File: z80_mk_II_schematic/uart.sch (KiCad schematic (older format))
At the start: 20 parts

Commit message: Lots more work on schematic
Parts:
- U22: renamed from U?; value 74LS32 -> 74LS365
- U24: renamed from U?; value 74LS32 -> D3-6402
- U25: renamed from U?; value 74LS32 -> 74LS139
- U27: renamed from U?; value 74LS32 -> MAX232
- gave numbers to parts that had none: 12
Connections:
- net ~UART_EN~ renamed ~UART_CE~

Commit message: Un-fsck something which made most of the chips into 74LS00 for some very odd reason. Also start to assign footprints.
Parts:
- R24: footprint (none) -> Resistors_ThroughHole:R_Axial_DIN0207_L6.3mm_D2.5mm_P10.16mm_Horizontal
- U22, U25: footprint (none) -> Housings_DIP:DIP-16_W7.62mm
- U23, U26: footprint (none) -> Housings_DIP:DIP-14_W7.62mm
- U24: footprint (none) -> Housings_DIP:DIP-40_W15.24mm_Socket
- U27: footprint (none) -> Housings_DIP:DIP-20_W7.62mm_Socket
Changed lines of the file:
@@
 F 0 "U24" H 5500 3800 50  0000 C CNN
 F 1 "D3-6402" H 5500 3700 50  0000 C CNN
-F 2 "" H 5500 2400 50  0001 C CNN
+F 2 "Housings_DIP:DIP-40_W15.24mm_Socket" H 5500 2400 50  0001 C CNN
 F 3 "" H 5450 2200 50  0001 C CNN
 	1    5500 3800
@@
 F 0 "U27" H 9100 3350 50  0000 C CNN
 F 1 "MAX232" H 9100 3250 50  0000 C CNN
-F 2 "" H 9200 1900 50  0001 L CNN
+F 2 "Housings_DIP:DIP-20_W7.62mm_Socket" H 9200 1900 50  0001 L CNN
 F 3 "" H 9150 3050 50  0001 C CNN
 	1    9150 2950
@@
 F 0 "U25" H 5500 5900 50  0000 C CNN
 F 1 "74LS139" H 5450 5800 50  0000 C CNN
-F 2 "" H 5500 5900 50  0001 C CNN
+F 2 "Housings_DIP:DIP-16_W7.62mm" H 5500 5900 50  0001 C CNN
 F 3 "" H 5500 5900 50  0001 C CNN
 	1    5500 5900
@@
 F 0 "U25" H 5500 6800 50  0000 C CNN
 F 1 "74LS139" H 5450 6700 50  0000 C CNN
-F 2 "" H 5500 6800 50  0001 C CNN
+F 2 "Housings_DIP:DIP-16_W7.62mm" H 5500 6800 50  0001 C CNN
 F 3 "" H 5500 6800 50  0001 C CNN
 	2    5500 6800
@@
 F 0 "U25" H 8980 5896 50  0000 L CNN
 F 1 "74LS139" H 8980 5805 50  0000 L CNN
-F 2 "" H 8750 5850 50  0001 C CNN
+F 2 "Housings_DIP:DIP-16_W7.62mm" H 8750 5850 50  0001 C CNN
 F 3 "" H 8750 5850 50  0001 C CNN
 	3    8750 5850
@@
 F 0 "U23" H 4200 6800 50  0000 C CNN
 F 1 "74LS32" H 4200 7034 50  0000 C CNN
-F 2 "" H 4200 6800 50  0001 C CNN
+F 2 "Housings_DIP:DIP-14_W7.62mm" H 4200 6800 50  0001 C CNN
 F 3 "http://www.ti.com/lit/gpn/sn74LS32" H 4200 6800 50  0001 C CNN
 	1    4200 6800
@@
 F 0 "U22" H 3150 4300 50  0000 C CNN
 F 1 "74LS365" H 3150 4200 50  0000 C CNN
-F 2 "" H 3150 4400 50  0001 C CNN
+F 2 "Housings_DIP:DIP-16_W7.62mm" H 3150 4400 50  0001 C CNN
 F 3 "" H 3150 4400 50  0001 C CNN
 	1    3150 4400
@@
 F 0 "R24" V 3554 5650 50  0000 C CNN
 F 1 "10K" V 3645 5650 50  0000 C CNN
-F 2 "" H 3750 5650 50  0001 C CNN
+F 2 "Resistors_ThroughHole:R_Axial_DIN0207_L6.3mm_D2.5mm_P10.16mm_Horizontal" H 3750 5650 50  0001 C CNN
 F 3 "~" H 3750 5650 50  0001 C CNN
 	1    3750 5650
@@
 F 0 "U23" H 4200 7350 50  0000 C CNN
 F 1 "74LS32" H 4200 7584 50  0000 C CNN
-F 2 "" H 4200 7350 50  0001 C CNN
+F 2 "Housings_DIP:DIP-14_W7.62mm" H 4200 7350 50  0001 C CNN
 F 3 "http://www.ti.com/lit/gpn/sn74LS32" H 4200 7350 50  0001 C CNN
 	4    4200 7350
@@
 F 0 "U23" H 9780 5896 50  0000 L CNN
 F 1 "74LS32" H 9780 5805 50  0000 L CNN
-F 2 "" H 9550 5850 50  0001 C CNN
+F 2 "Housings_DIP:DIP-14_W7.62mm" H 9550 5850 50  0001 C CNN
 F 3 "http://www.ti.com/lit/gpn/sn74LS32" H 9550 5850 50  0001 C CNN
 	5    9550 5850
@@
 F 0 "U26" V 6450 6100 50  0000 R CNN
 F 1 "74LS00" H 6550 5750 50  0000 R CNN
-F 2 "" H 6450 6000 50  0001 C CNN
+F 2 "Housings_DIP:DIP-14_W7.62mm" H 6450 6000 50  0001 C CNN
 F 3 "http://www.ti.com/lit/gpn/sn74ls00" H 6450 6000 50  0001 C CNN
 	3    6450 6000

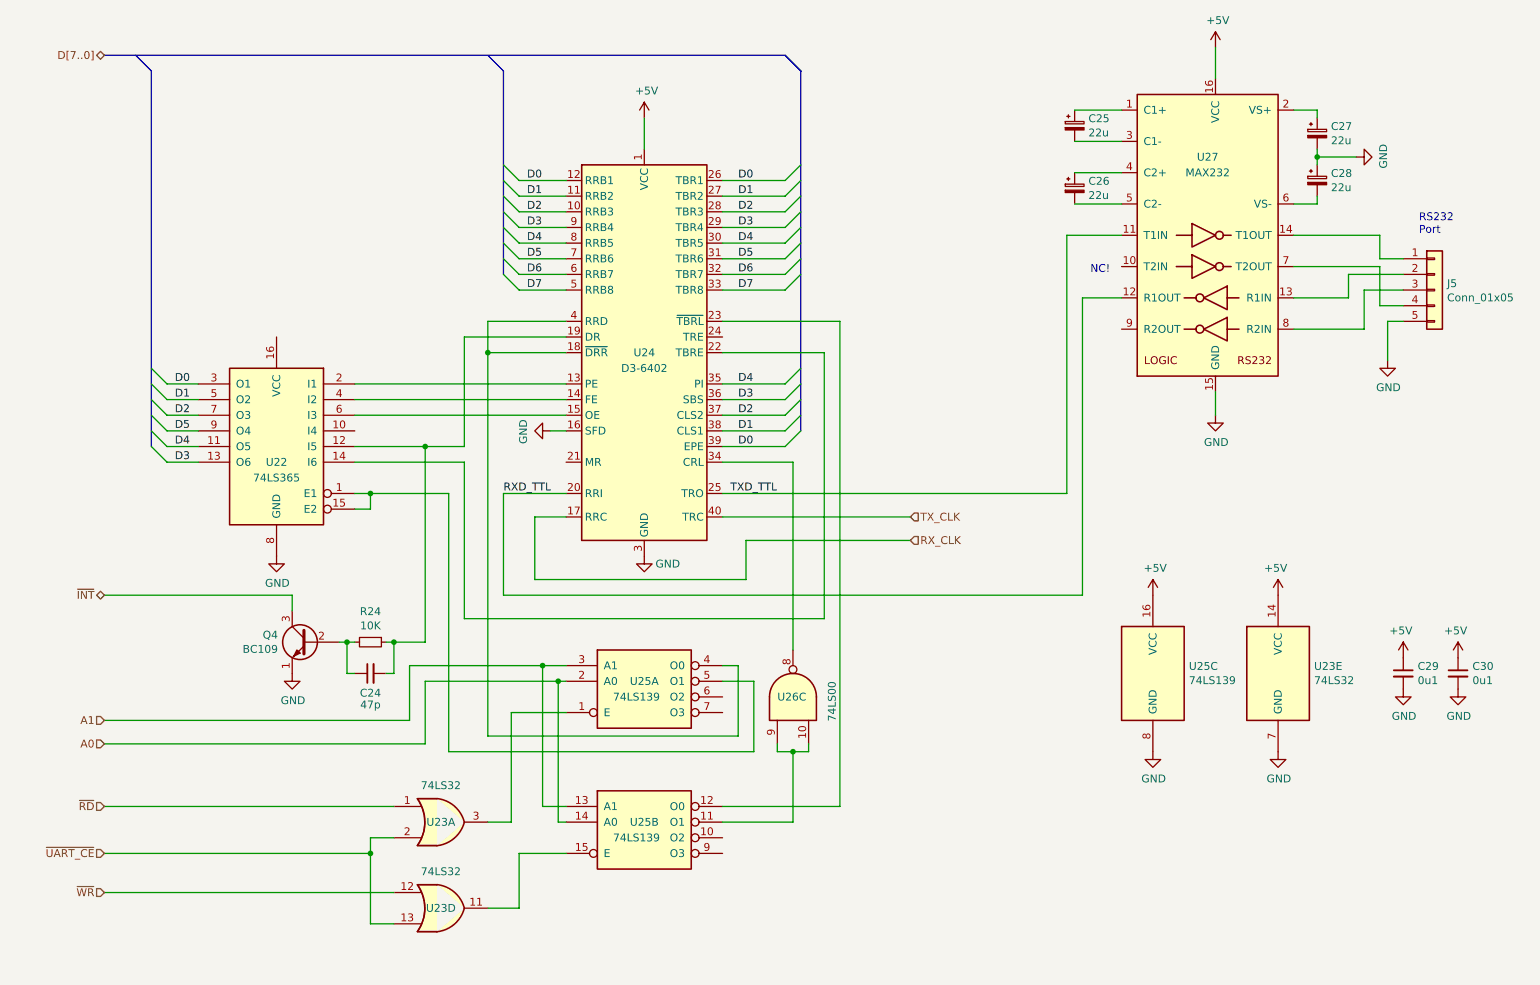
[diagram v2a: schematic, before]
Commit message: Add some missing gates and wiring.
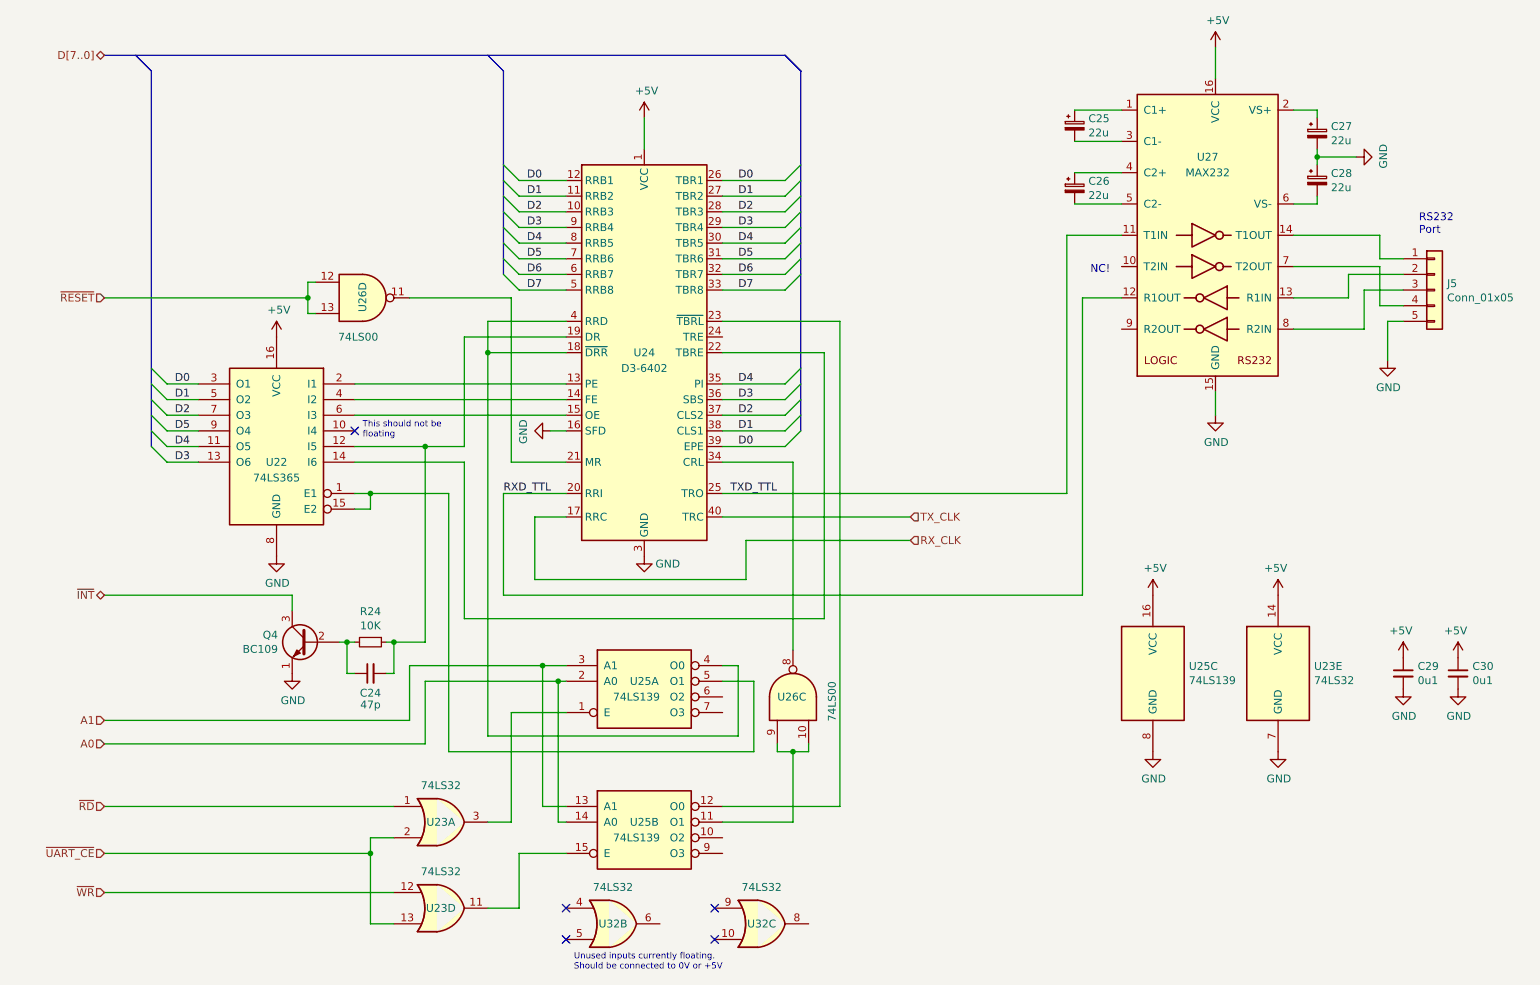
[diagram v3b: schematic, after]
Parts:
- added unit 4 of U26
- added U32: 74LS32, Housings_DIP:DIP-14_W7.62mm, symbol 74xx:74LS32
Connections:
- net +5V: now also U22.16 (VCC)
- net at U24.21 (MR): now also U26.11
- new net ~RESET~: U26.12, U26.13
- no-connect marks 0 -> 5
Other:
- note added: "This should not be\nfloating"
- note added: "Unused inputs currently floating.\nShould be connected to 0V or +5V"
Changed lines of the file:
@@
 	0    -1   -1   0
 $EndComp
+$Comp
+L 74xx:74LS32 U32
+U 2 1 5F9F56CD
+P 5300 7450
+F 0 "U32" H 5300 7450 50  0000 C CNN
+F 1 "74LS32" H 5300 7684 50  0000 C CNN
+F 2 "Housings_DIP:DIP-14_W7.62mm" H 5300 7450 50  0001 C CNN
+F 3 "http://www.ti.com/lit/gpn/sn74LS32" H 5300 7450 50  0001 C CNN
+	2    5300 7450
+	1    0    0    -1
+$EndComp
+$Comp
+L 74xx:74LS32 U32
+U 3 1 5F9F777F
+P 6250 7450
+F 0 "U32" H 6250 7450 50  0000 C CNN
+F 1 "74LS32" H 6250 7684 50  0000 C CNN
+F 2 "Housings_DIP:DIP-14_W7.62mm" H 6250 7450 50  0001 C CNN
+F 3 "http://www.ti.com/lit/gpn/sn74LS32" H 6250 7450 50  0001 C CNN
+	3    6250 7450
+	1    0    0    -1
+$EndComp
+NoConn ~ 5950 7550
+NoConn ~ 5950 7350
+NoConn ~ 5000 7550
+NoConn ~ 5000 7350
+Text Notes 5050 7750 0    40   ~ 0
+Unused inputs currently floating.\nShould be connected to 0V or +5V
+$Comp
+L 74xx:74LS00 U26
+U 4 1 5FD3BF49
+P 3700 3450
+F 0 "U26" V 3700 3550 50  0000 R CNN
+F 1 "74LS00" H 3800 3200 50  0000 R CNN
+F 2 "Housings_DIP:DIP-14_W7.62mm" H 3700 3450 50  0001 C CNN
+F 3 "http://www.ti.com/lit/gpn/sn74ls00" H 3700 3450 50  0001 C CNN
+	4    3700 3450
+	1    0    0    -1
+$EndComp
+Wire Wire Line
+	3400 3350 3350 3350
+Wire Wire Line
+	3350 3350 3350 3450
+Wire Wire Line
+	3350 3550 3400 3550
+Wire Wire Line
+	4650 4500 5000 4500
+Wire Wire Line
+	4000 3450 4650 3450
+Wire Wire Line
+	4650 3450 4650 4500
+$Comp
+L power:+5V #PWR0118
+U 1 1 5FD709B6
+P 3150 3700
+F 0 "#PWR0118" H 3150 3550 50  0001 C CNN
+F 1 "+5V" H 3165 3873 50  0000 C CNN
+F 2 "" H 3150 3700 50  0001 C CNN
+F 3 "" H 3150 3700 50  0001 C CNN
+	1    3150 3700
+	1    0    0    -1
+$EndComp
+Text HLabel 2050 3450 0    50   Input ~ 0
+~RESET~
+Wire Wire Line
+	2050 3450 3350 3450
+Connection ~ 3350 3450
+Wire Wire Line
+	3350 3450 3350 3550
+NoConn ~ 3650 4300
 Wire Bus Line
 	2050 1900 6400 1900
@@
 Wire Bus Line
 	6500 2000 6500 4300
+Text Notes 3700 4350 0    40   ~ 0
+This should not be\nfloating
 $EndSCHEMATC
